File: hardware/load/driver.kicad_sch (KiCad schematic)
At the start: 8 parts, among them J5 B2B-XH-A, Q1 DMG2301L, Q2 MMBT3904

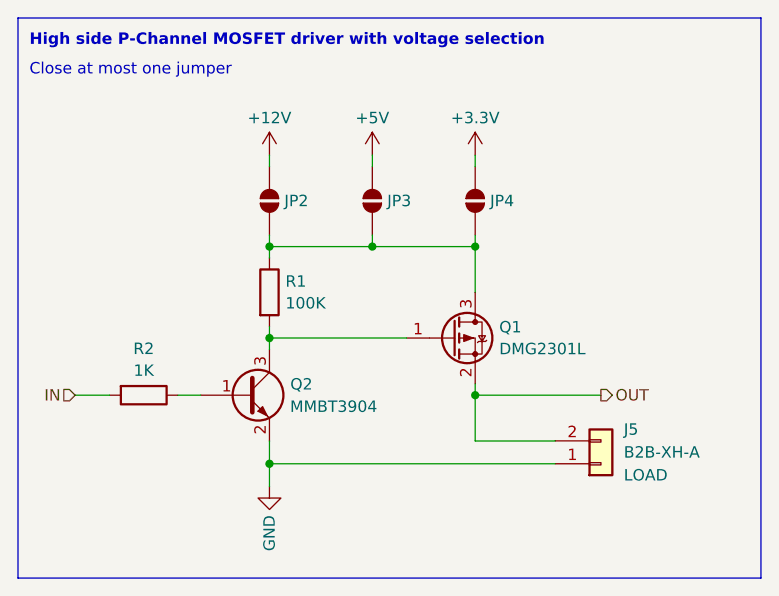
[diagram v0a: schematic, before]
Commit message: Abandon load accessory design, update errata.
Decided to abandon this design because it is overly complex and
doesn't work with addressable LEDs as intended.  It would be better
to design simpler boards for each use-case instead of having lots
of jumpers.
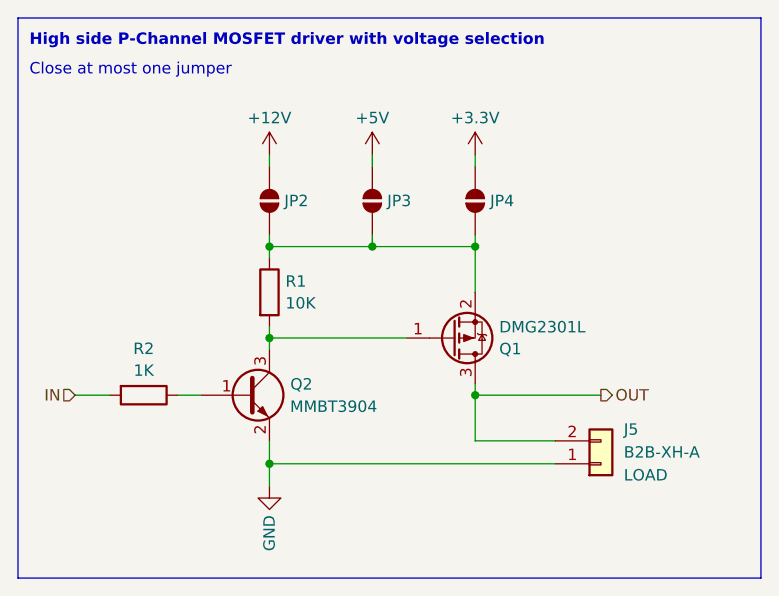
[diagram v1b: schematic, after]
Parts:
- R1: value 100K -> 10K
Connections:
- net OUT: now also Q1.3 (D); no longer Q1.2 (S)
- net at JP2.2 (B), JP3.2 (B), JP4.2 (B)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: now also Q1.2 (S); no longer Q1.3 (D)
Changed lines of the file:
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@@
 			)
 		)
-		(property "Value" "100K"
+		(property "Value" "10K"
 			(at 140.208 90.1121 0)
 			(effects
@@
 		(lib_id "Device:Q_PMOS_GSD")
 		(at 158.75 93.98 0)
+		(mirror x)
 		(unit 1)
 		(exclude_from_sim no)
@@
 		(dnp no)
 		(property "Reference" "Q1"
-			(at 163.957 92.7678 0)
+			(at 163.957 95.1922 0)
 			(effects
 				(font
@@
 		)
 		(property "Value" "DMG2301L"
-			(at 163.957 95.1921 0)
+			(at 163.957 92.7679 0)
 			(effects
 				(font
@@
 		)
 		(property "Footprint" "Package_TO_SOT_SMD:SOT-23_Handsoldering"
-			(at 163.83 91.44 0)
+			(at 163.83 96.52 0)
 			(effects
 				(font
